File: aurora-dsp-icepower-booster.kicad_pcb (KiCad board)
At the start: 2 copper layers, 180 x 200 mm, 268 parts, among them J1 24V DC, J10 XLR3_OUT, J11 XLR3_OUT, J12 XLR3_OUT, J13 XLR3_OUT, J14 XLR3_OUT, J2 REMOTE 3.5mm, J3 XLR_IN_1, J4 XLR_IN_2, J5 XLR_IN_3, J6 XLR_IN_4, J7 XLR_IN_5, J8 XLR_IN_6, J9 XLR3_OUT, Q1 BSS138, Q2 BSS138, Q3 BSS138, Q4 BSS138, Q5 BSS138, Q6 BSS138, Q7 BSS138, SW1 ALWAYS/REMOTE, SW2 Gain CH1, SW3 Gain CH2, SW4 Gain CH3, SW5 Gain CH4, SW6 Gain CH5, SW7 Gain CH6, U1 TEL5-2422, U10 LM4562, U11 LM4562, U12 LM4562, U13 LM4562, U14 ADP7118ARDZ-11, U15 ADP7182AUJZ-11, U2 LM4562, U3 LM4562, U4 LM4562, U5 LM4562, U6 LM4562, U7 LM4562, U8 LM4562, U9 LM4562

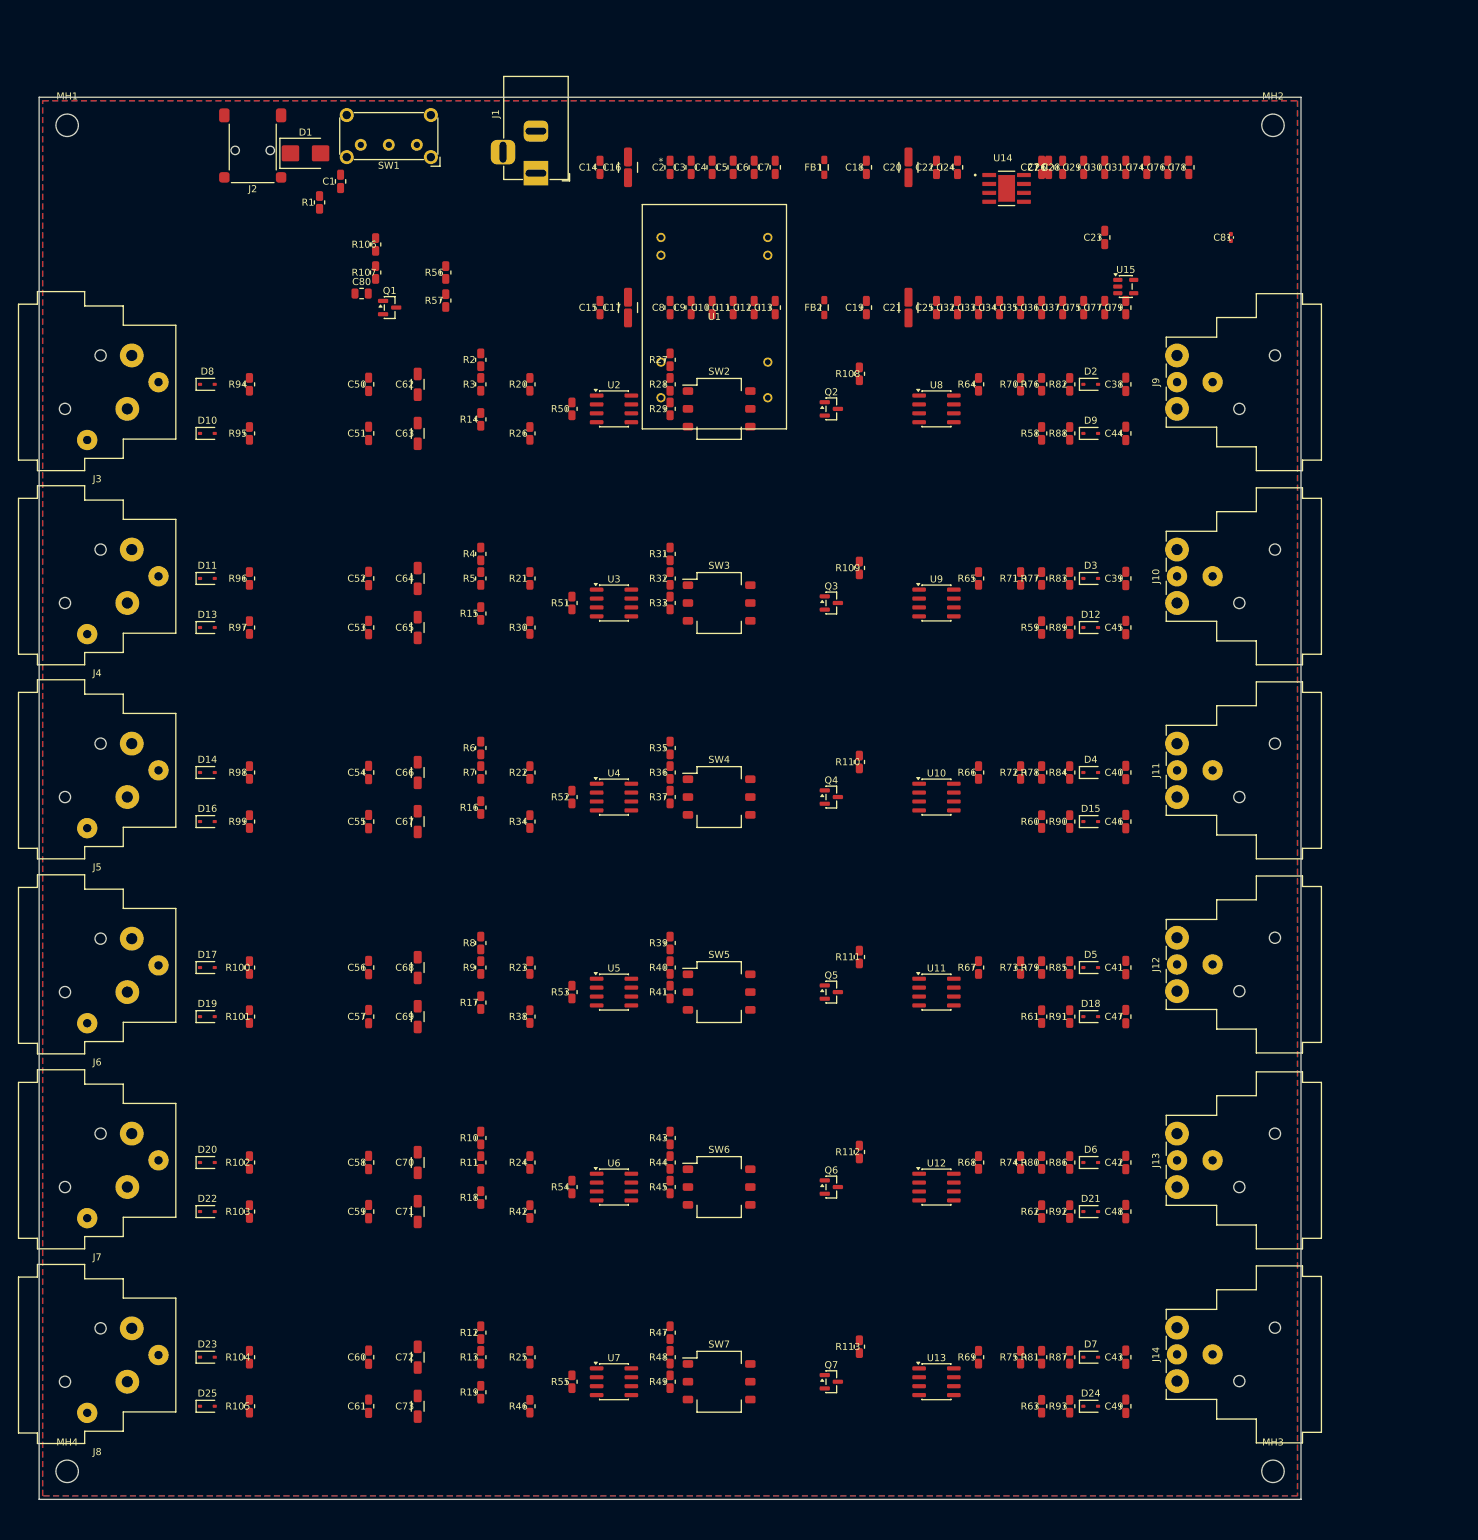
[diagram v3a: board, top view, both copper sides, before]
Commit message: Narrow board to 158mm: 0 DRC errors, POWER_ZONE reorganized
Board: 180x200 → 158x200mm (XLR outputs define right edge)

X columns compressed:
- X_EMI_R 27→29 (TVS clearance)
- X_GAIN_R 64→61 (RX_IC clearance)
- X_OUT_TVS 124→126 (prot-R separation)
- X_OUT_DEC 128→130

POWER_ZONE complete reorganization:
- U1 TEL5: (110,19,90°) — rotated to avoid CH1 collision
- U14 ADP7118: (146,4) — clear of MH2
- U15 ADP7182: (125,25) — below U1
- V+ 4 rows: Row A y=8 x=78..99, Row B y=25 x=106..121,
  Row C y=10 x=139..148, Row D y=14 x=139..145
- V- single row y=32 x=69..129 (21 caps, 3mm pitch)
- D1 (40,20), C81 (141,4) — relocated for clearance
- FB1/FB2 separated to avoid cap collisions

classify_function adjustments:
- GAIN_FB offset -6→-4 (driver IC clearance)
- Output prot R offset +4→+3 (TVS clearance)

DRC: 0 errors, 0 shorts, 0 courtyard overlaps, 499 unconnected (unrouted)
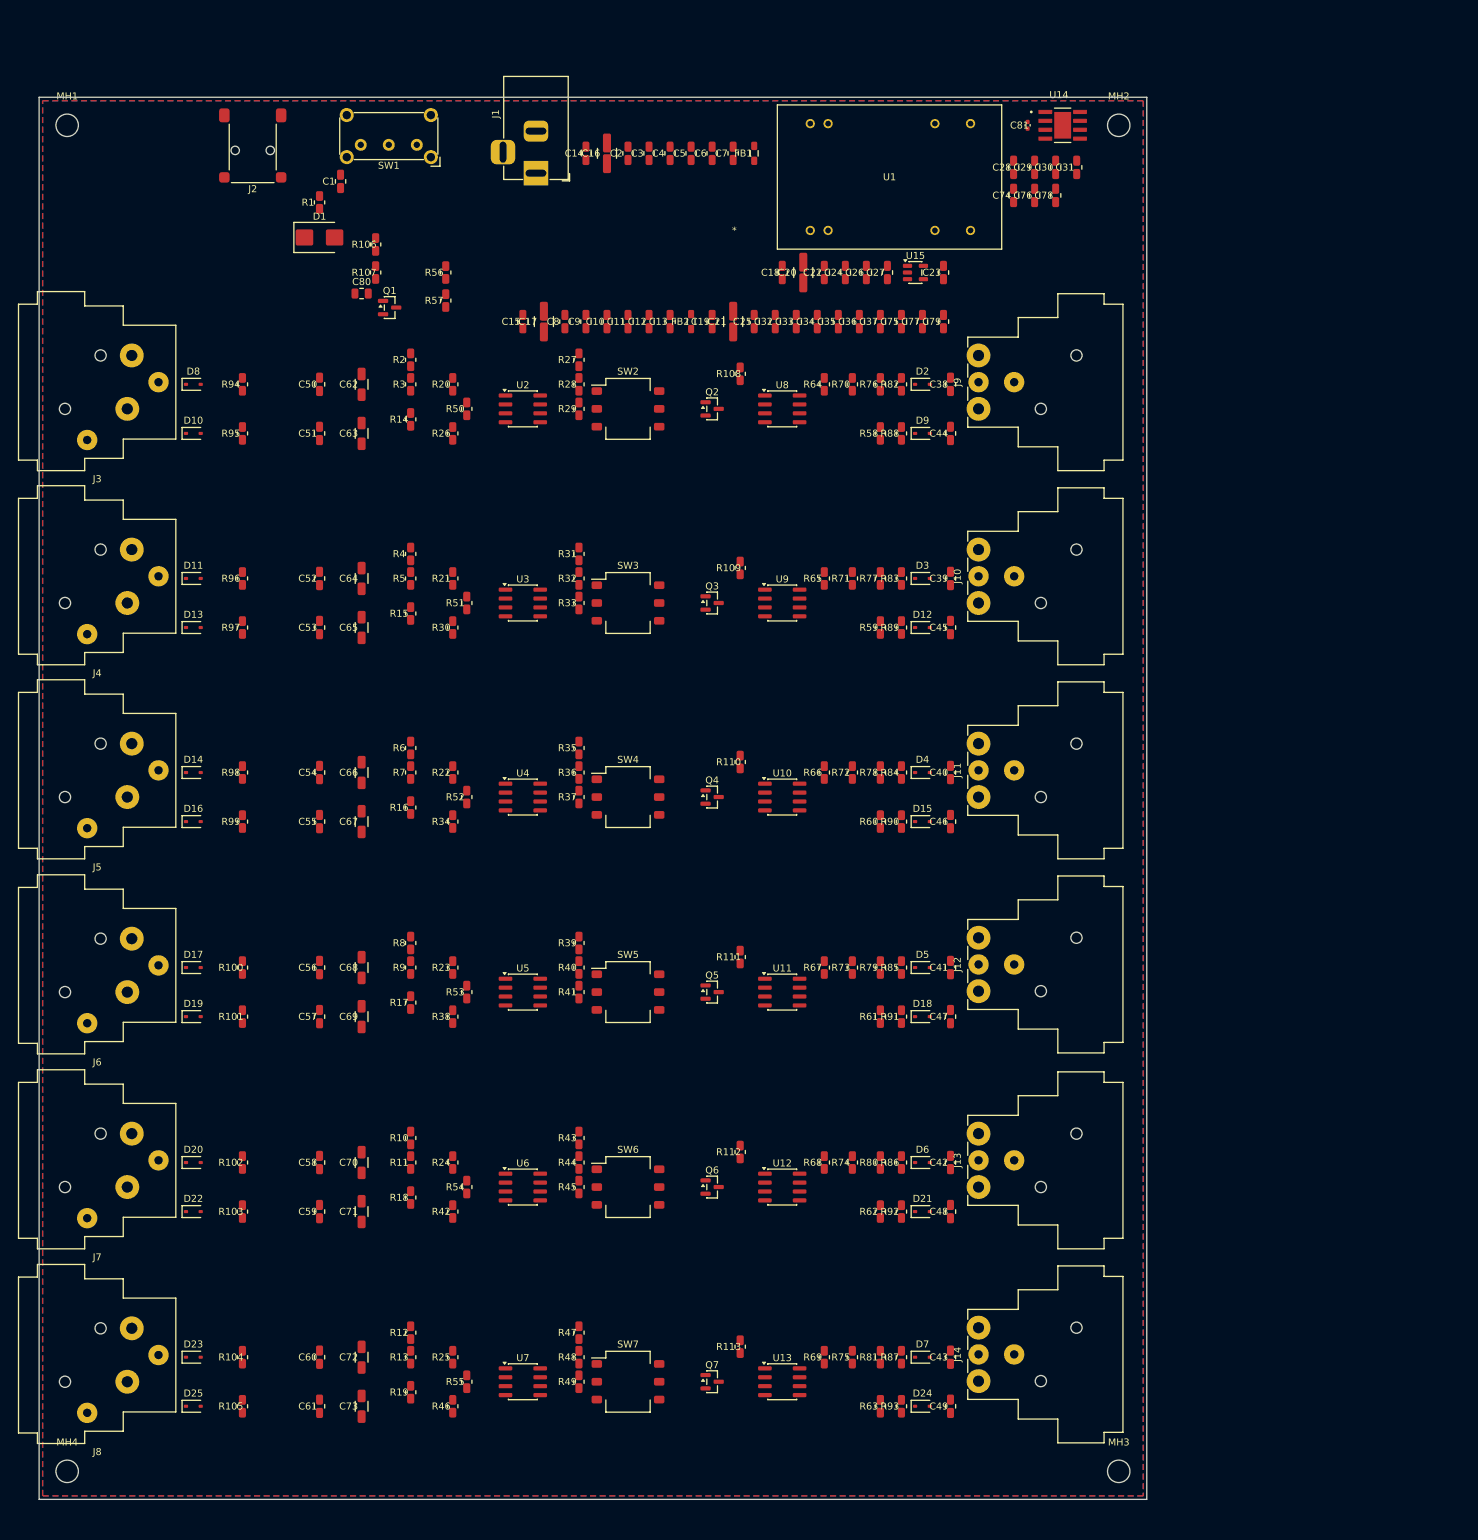
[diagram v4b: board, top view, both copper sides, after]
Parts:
- moved C81 33.1 mm to (141.0, 4.00)
- moved U15 30.1 mm to (125.0, 25.0)
- moved C26 30.0 mm to (118.0, 25.0)
- moved J10 28.3 mm to (134.0, 72.1)
- moved J11 28.3 mm to (134.0, 99.8)
- moved J12 28.3 mm to (134.0, 127.5)
- moved J13 28.3 mm to (134.0, 155.4)
- moved J14 28.3 mm to (134.0, 183.1)
- moved J9 28.3 mm to (134.0, 44.5)
- moved C27 26.6 mm to (121.0, 25.0)
- moved C25 26.1 mm to (102.0, 32.0)
- moved C32 26.1 mm to (105.0, 32.0)
- moved C33 26.1 mm to (108.0, 32.0)
- moved C34 26.1 mm to (111.0, 32.0)
- moved C35 26.1 mm to (114.0, 32.0)
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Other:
- board size 180 x 200 mm -> 158 x 200 mm

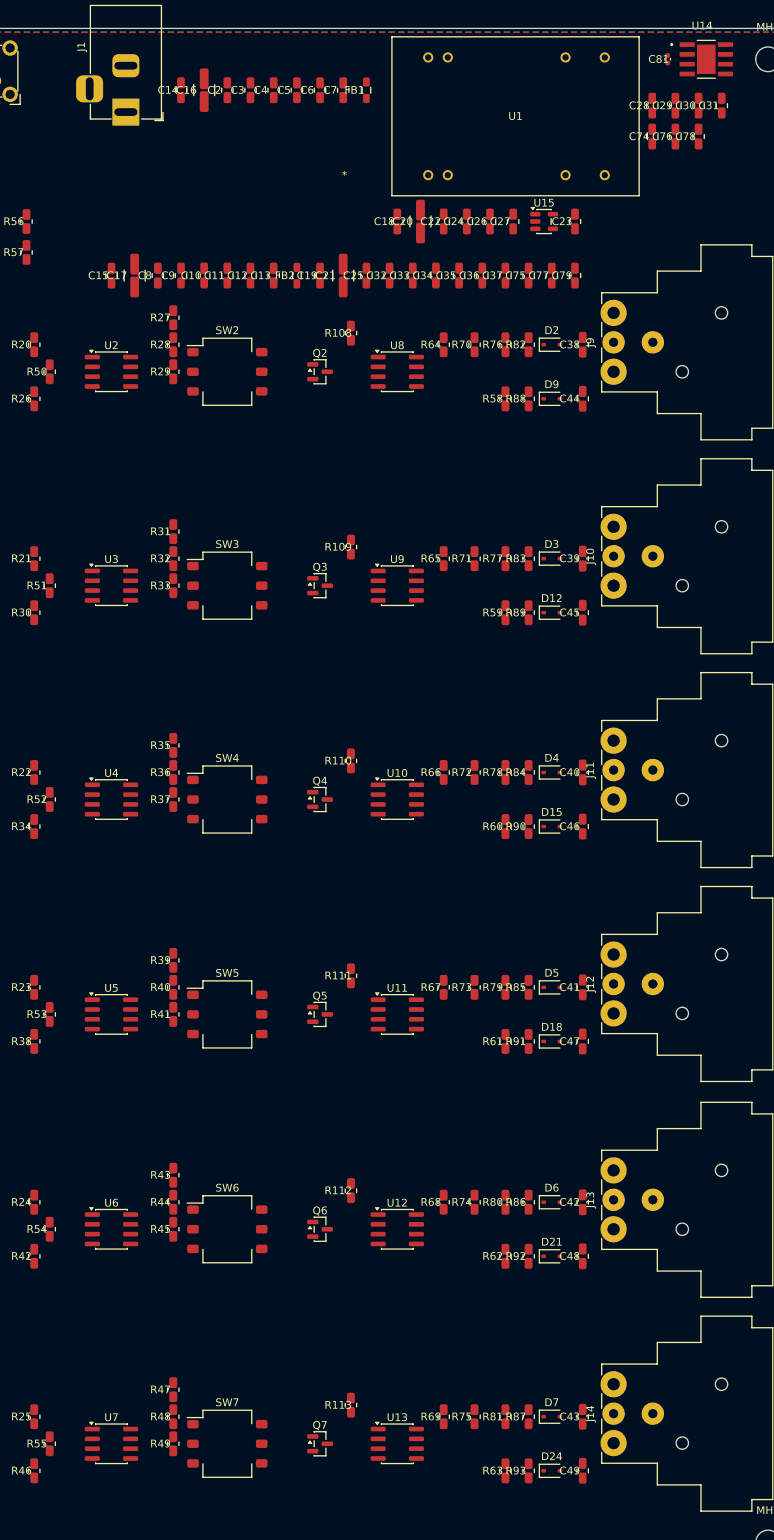
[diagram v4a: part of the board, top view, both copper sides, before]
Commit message: IC-adjacent bypass caps per copilot-instructions.md
Bypass cap placement:
- 100nF caps at IC_x±2.5, CH_Y∓4.7 (above/below IC body)
- Pin-to-cap distance 2.6-3.0mm (spec: <3mm from IC pin)
- All 12 LM4562 ICs pass CHECK 1 (was: 15 failures at 12-61mm)

Bulk cap distribution:
- 10µF distributed between Rx channel pairs (x=75/64, y=58/114/169)
- C20/C21 100µF moved to driver center (x=111/101, y=114)
- 9/12 ICs pass CHECK 2 (<20mm); 3 drivers need schematic add

Audit tool improvements:
- Pin-based distance measurement for SOIC-8/SOT-23-5
- Proper rotation handling for supply pin positions

DRC: 0 shorts, 0 clearance, 2 cosmetic courtyard warnings (U1 TEL5)
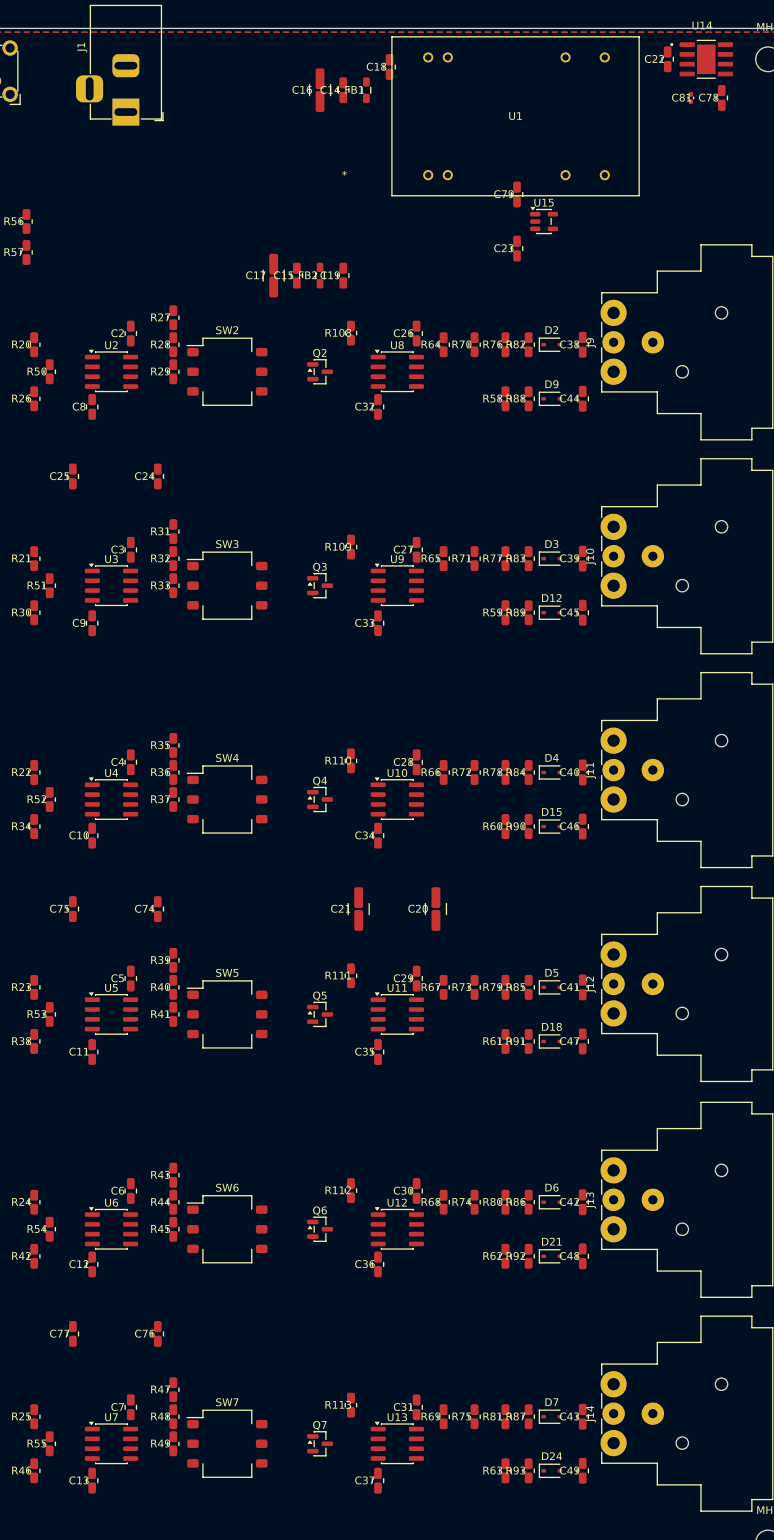
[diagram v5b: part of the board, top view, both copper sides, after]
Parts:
- moved C31 173.1 mm to (108.5, 178.5)
- moved C7 172.7 mm to (71.5, 178.5)
- moved C76 168.9 mm to (75.0, 169.0)
- moved C13 157.8 mm to (66.5, 188.0)
- moved C37 156.9 mm to (103.5, 188.0)
- moved C77 150.4 mm to (64.0, 169.0)
- moved C30 145.2 mm to (108.5, 150.5)
- moved C6 144.6 mm to (71.5, 150.5)
- moved C12 129.6 mm to (66.5, 160.0)
- moved C36 128.7 mm to (103.5, 160.0)
- moved C74 118.7 mm to (75.0, 114.0)
- moved C29 117.9 mm to (108.5, 123.0)
- moved C5 117.0 mm to (71.5, 123.0)
- moved C11 102.0 mm to (66.5, 132.5)
- moved C35 101.0 mm to (103.5, 132.5)
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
